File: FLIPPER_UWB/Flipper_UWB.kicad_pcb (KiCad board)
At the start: 2 copper layers, 34 x 67 mm, 13 parts, among them IC1 DWM1000, J1 Conn_01x08_Socket, J2 Conn_01x10_Socket

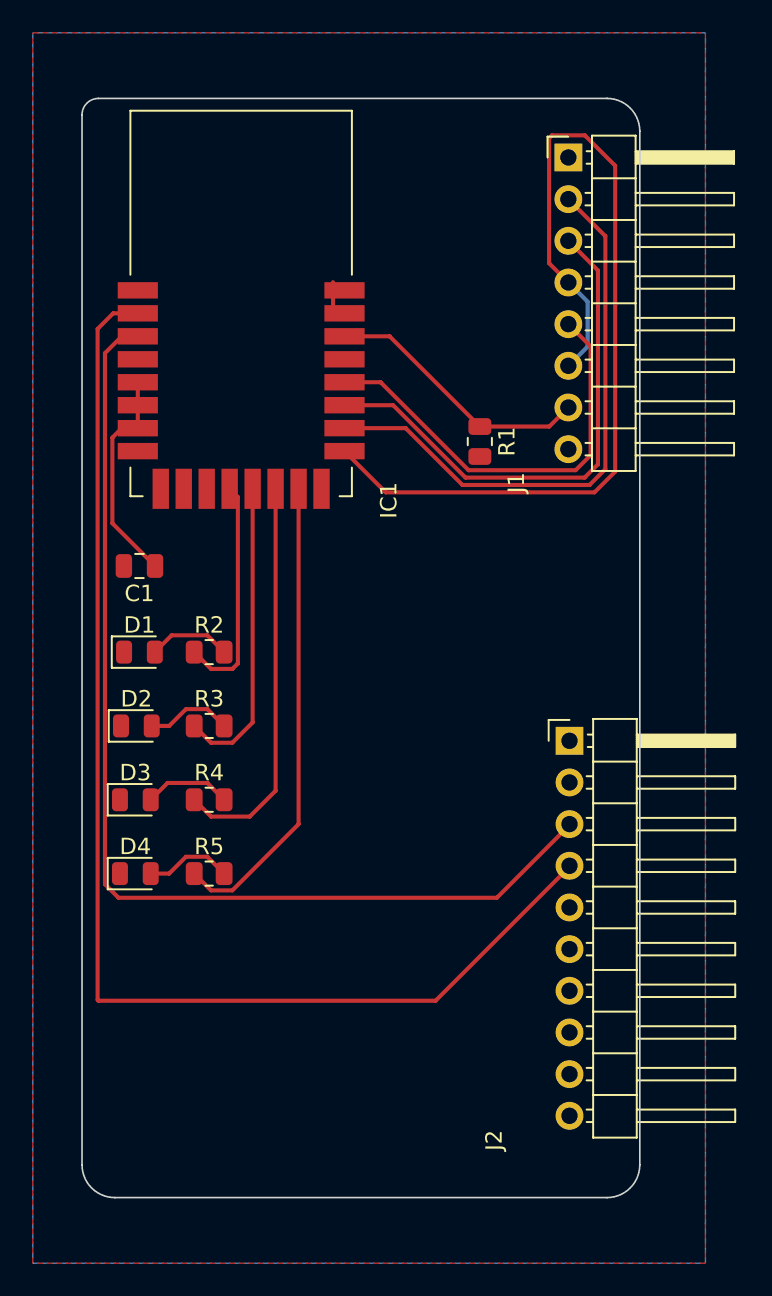
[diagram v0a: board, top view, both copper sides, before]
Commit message: Update Flipper_UWB pcb
Corrected PCB
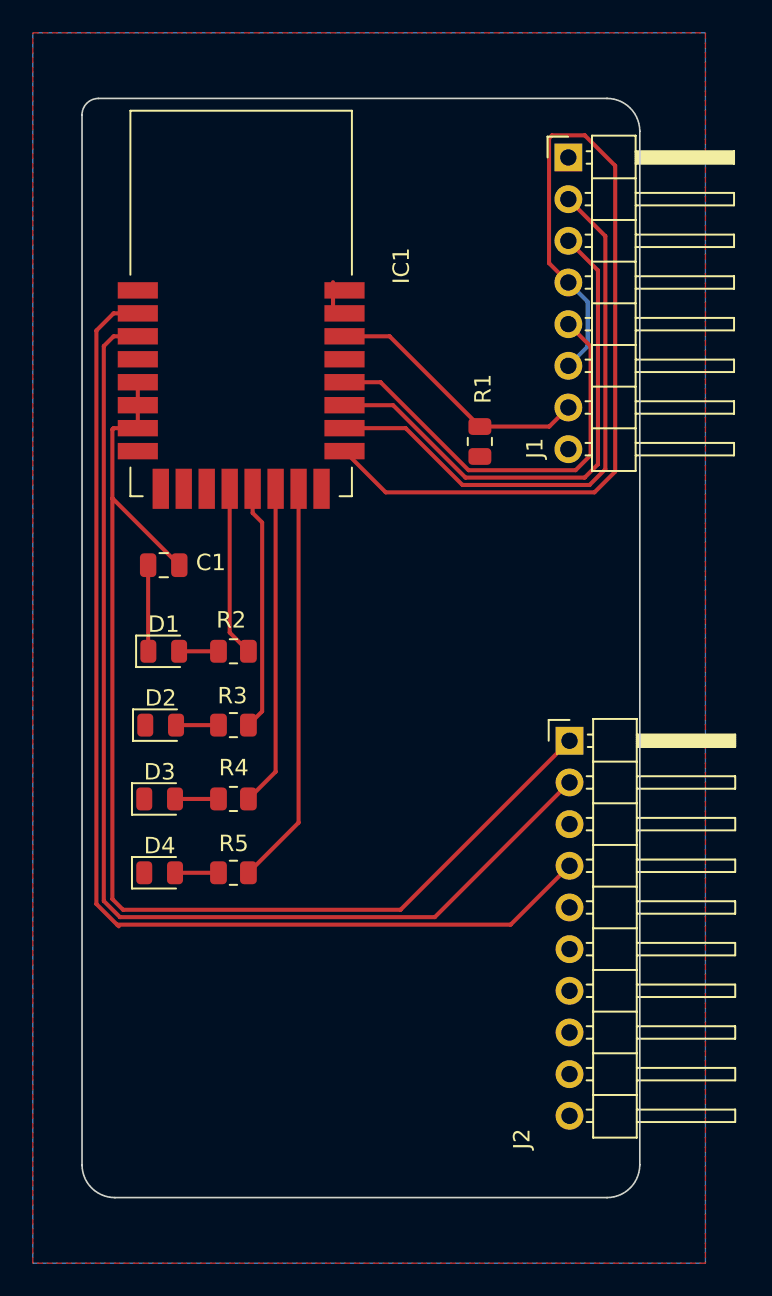
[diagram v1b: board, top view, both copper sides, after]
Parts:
- moved C1 1.48 mm to (129.0, 91.5)
- moved D1 1.48 mm to (129.0, 96.7)
- moved D2 1.48 mm to (128.8, 101.2)
- moved D3 1.48 mm to (128.7, 105.7)
- moved D4 1.48 mm to (128.7, 110.2)
- moved R2 1.48 mm to (133.2, 96.7), turned to 180 degrees
- moved R3 1.48 mm to (133.2, 101.2), turned to 180 degrees
- moved R4 1.48 mm to (133.2, 105.7), turned to 180 degrees
- moved R5 1.48 mm to (133.2, 110.2), turned to 180 degrees
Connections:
- J2 pad 1: unconnected-(J2-Pin_1-Pad1) -> +3.3V
- J2 pad 2: GND -> /RSTN
- J2 pad 3: /RSTN -> GND
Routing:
- net +3.3V: track 13.5 -> 71.2 mm
- net /WKP: track 75.8 -> 68.9 mm
- net GND: track 1.40 -> 6.66 mm
- net /LED3: track 24.4 -> 19.6 mm
- net /LED4: track 28.9 -> 24.7 mm
- net /LED2: track 18.7 -> 15.0 mm
- net /LED1: track 14.1 -> 10.9 mm
- net /RSTN: track 65.2 -> 68.3 mm
- net Net-(D4-A): track 5.32 -> 2.65 mm
- net Net-(D3-A): track 5.32 -> 2.65 mm
- net Net-(D2-A): track 5.26 -> 2.59 mm
- net Net-(D1-A): track 5.07 -> 2.40 mm

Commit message: Update and correction shield UWB
Update and correction of the Flipper Zero UWB shield.
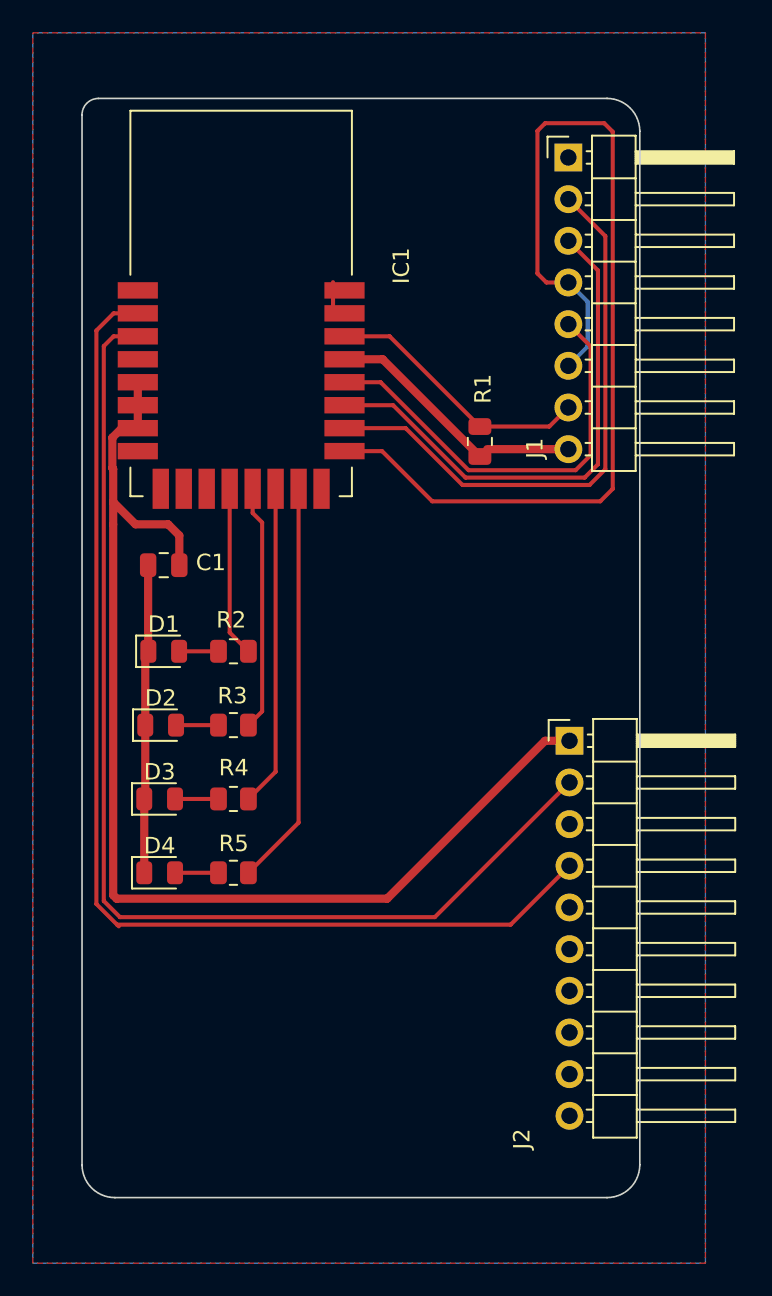
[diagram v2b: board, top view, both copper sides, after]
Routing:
- net GND: track 6.66 -> 36.5 mm
- net /CS: track 56.9 -> 61.6 mm
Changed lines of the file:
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@@
   (segment (start 153.715 104.695) (end 145.504 112.906) (width 0.25) (layer "F.Cu") (net 3))
   (segment (start 125.326 111.918396) (end 125.326 78.099) (width 0.25) (layer "F.Cu") (net 3))
-  (segment (start 127.4 80.3) (end 127.4 81.7) (width 0.25) (layer "F.Cu") (net 5))
-  (segment (start 143.414 112.456) (end 153.715 102.155) (width 0.25) (layer "F.Cu") (net 5))
-  (segment (start 125.85 83.175) (end 125.85 87.37) (width 0.25) (layer "F.Cu") (net 5))
-  (segment (start 125.85 87.37) (end 129.9305 91.4505) (width 0.25) (layer "F.Cu") (net 5))
-  (segment (start 125.925 83.1) (end 125.85 83.175) (width 0.25) (layer "F.Cu") (net 5))
-  (segment (start 126.5 112.456) (end 143.414 112.456) (width 0.25) (layer "F.Cu") (net 5))
-  (segment (start 127.4 81.7) (end 127.4 83.1) (width 0.25) (layer "F.Cu") (net 5))
-  (segment (start 127.4 83.1) (end 125.925 83.1) (width 0.25) (layer "F.Cu") (net 5))
-  (segment (start 125.85 111.806) (end 126.5 112.456) (width 0.25) (layer "F.Cu") (net 5))
-  (segment (start 125.85 87.37) (end 125.85 111.806) (width 0.25) (layer "F.Cu") (net 5))
+  (segment (start 152.225 102.155) (end 142.6 111.78) (width 0.5) (layer "F.Cu") (net 5))
+  (segment (start 126.425 83.1) (end 127.4 83.1) (width 0.5) (layer "F.Cu") (net 5))
+  (segment (start 126.11 111.78) (end 125.9 111.57) (width 0.5) (layer "F.Cu") (net 5))
+  (segment (start 129.9305 89.6405) (end 129.25 88.96) (width 0.5) (layer "F.Cu") (net 5))
+  (segment (start 127.4 80.3) (end 127.4 81.7) (width 0.5) (layer "F.Cu") (net 5))
+  (segment (start 125.85 85.54) (end 125.85 83.675) (width 0.5) (layer "F.Cu") (net 5))
+  (segment (start 125.9 111.57) (end 125.9 88.96) (width 0.5) (layer "F.Cu") (net 5))
+  (segment (start 125.85 83.675) (end 126.425 83.1) (width 0.5) (layer "F.Cu") (net 5))
+  (segment (start 153.715 102.155) (end 152.225 102.155) (width 0.5) (layer "F.Cu") (net 5))
+  (segment (start 129.9305 91.4505) (end 129.9305 89.6405) (width 0.5) (layer "F.Cu") (net 5))
+  (segment (start 142.6 111.78) (end 126.11 111.78) (width 0.5) (layer "F.Cu") (net 5))
+  (segment (start 125.9 85.59) (end 125.85 85.54) (width 0.5) (layer "F.Cu") (net 5))
+  (segment (start 129.25 88.96) (end 127.26 88.96) (width 0.5) (layer "F.Cu") (net 5))
+  (segment (start 127.4 81.7) (end 127.4 83.1) (width 0.5) (layer "F.Cu") (net 5))
+  (segment (start 125.9 88.96) (end 125.9 87.6) (width 0.5) (layer "F.Cu") (net 5))
+  (segment (start 125.9 87.6) (end 125.9 85.59) (width 0.5) (layer "F.Cu") (net 5))
+  (segment (start 127.26 88.96) (end 125.9 87.6) (width 0.5) (layer "F.Cu") (net 5))
+  (segment (start 148.25 84.825) (end 148.6962 84.3788) (width 0.25) (layer "F.Cu") (net 6))
+  (segment (start 148.6962 84.3788) (end 153.6446 84.3788) (width 0.5) (layer "F.Cu") (net 6))
+  (segment (start 140 78.9) (end 142.325 78.9) (width 0.5) (layer "F.Cu") (net 6))
+  (segment (start 127.8555 101.2005) (end 127.8555 105.638) (width 0.5) (layer "F.Cu") (net 6))
+  (segment (start 142.325 78.9) (end 148.25 84.825) (width 0.5) (layer "F.Cu") (net 6))
   (segment (start 128.043 96.7005) (end 128.0305 96.688) (width 0.25) (layer "F.Cu") (net 6))
   (segment (start 139.3 74.2012) (end 139.3 75.6012) (width 0.25) (layer "F.Cu") (net 6))
-  (segment (start 128.0305 96.688) (end 128.0305 91.4505) (width 0.25) (layer "F.Cu") (net 6))
+  (segment (start 127.8555 105.638) (end 127.793 105.7005) (width 0.25) (layer "F.Cu") (net 6))
+  (segment (start 127.793 110.2005) (end 127.793 105.7005) (width 0.5) (layer "F.Cu") (net 6))
+  (segment (start 128.0305 96.688) (end 128.0305 91.4505) (width 0.5) (layer "F.Cu") (net 6))
+  (segment (start 127.8555 96.863) (end 127.8555 101.2005) (width 0.5) (layer "F.Cu") (net 6))
+  (segment (start 128.0305 96.688) (end 127.8555 96.863) (width 0.25) (layer "F.Cu") (net 6))
   (segment (start 129.7305 101.2005) (end 132.318 101.2005) (width 0.25) (layer "F.Cu") (net 10))
   (segment (start 129.668 105.7005) (end 132.318 105.7005) (width 0.25) (layer "F.Cu") (net 11))
@@
   (segment (start 124.876 112.104792) (end 126.239208 113.468) (width 0.25) (layer "F.Cu") (net 13))
   (segment (start 124.876 77.149) (end 124.876 112.104792) (width 0.25) (layer "F.Cu") (net 13))
-  (segment (start 156.5 85.75) (end 156.5 67.1042) (width 0.25) (layer "F.Cu") (net 14))
-  (segment (start 152.4696 65.4238) (end 152.4696 73.0438) (width 0.25) (layer "F.Cu") (net 14))
-  (segment (start 154.6458 65.25) (end 152.6434 65.25) (width 0.25) (layer "F.Cu") (net 14))
-  (segment (start 156.5 67.1042) (end 154.6458 65.25) (width 0.25) (layer "F.Cu") (net 14))
-  (segment (start 152.6434 65.25) (end 152.4696 65.4238) (width 0.25) (layer "F.Cu") (net 14))
-  (segment (start 140 84.4988) (end 142.5137 87.0125) (width 0.25) (layer "F.Cu") (net 14))
-  (segment (start 155.2375 87.0125) (end 156.5 85.75) (width 0.25) (layer "F.Cu") (net 14))
-  (segment (start 142.5137 87.0125) (end 155.2375 87.0125) (width 0.25) (layer "F.Cu") (net 14))
-  (segment (start 152.4696 73.0438) (end 153.6446 74.2188) (width 0.25) (layer "F.Cu") (net 14))
+  (segment (start 155.59 87.56) (end 156.35 86.8) (width 0.25) (layer "F.Cu") (net 14))
+  (segment (start 155.83 64.51) (end 152.23 64.51) (width 0.25) (layer "F.Cu") (net 14))
+  (segment (start 142.2888 84.4988) (end 145.35 87.56) (width 0.25) (layer "F.Cu") (net 14))
+  (segment (start 151.76 73.67) (end 152.3088 74.2188) (width 0.25) (layer "F.Cu") (net 14))
+  (segment (start 140 84.4988) (end 142.2888 84.4988) (width 0.25) (layer "F.Cu") (net 14))
+  (segment (start 145.35 87.56) (end 155.59 87.56) (width 0.25) (layer "F.Cu") (net 14))
+  (segment (start 151.76 64.98) (end 151.76 73.67) (width 0.25) (layer "F.Cu") (net 14))
+  (segment (start 156.35 86.8) (end 156.35 65.03) (width 0.25) (layer "F.Cu") (net 14))
+  (segment (start 152.23 64.51) (end 151.76 64.98) (width 0.25) (layer "F.Cu") (net 14))
+  (segment (start 156.35 65.03) (end 155.83 64.51) (width 0.25) (layer "F.Cu") (net 14))
+  (segment (start 152.3088 74.2188) (end 153.6446 74.2188) (width 0.25) (layer "F.Cu") (net 14))
   (segment (start 153.6446 74.2188) (end 154.8196 75.3938) (width 0.25) (layer "B.Cu") (net 14))
   (segment (start 154.8196 75.3938) (end 154.8196 78.1238) (width 0.25) (layer "B.Cu") (net 14))
@@
   (zone (net 6) (net_name "GND") (layer "F.Cu") (hatch edge 0.5)
     (connect_pads (clearance 0.5))
-    (min_thickness 0.25) (filled_areas_thickness no)
+    (min_thickness 0.5) (filled_areas_thickness no)
     (fill yes (thermal_gap 0.5) (thermal_bridge_width 0.5))
     (polygon

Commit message: Correction of the PCB and the schematic
Correction of the PCB and the schematic of the UBW shield for the FlipperZero
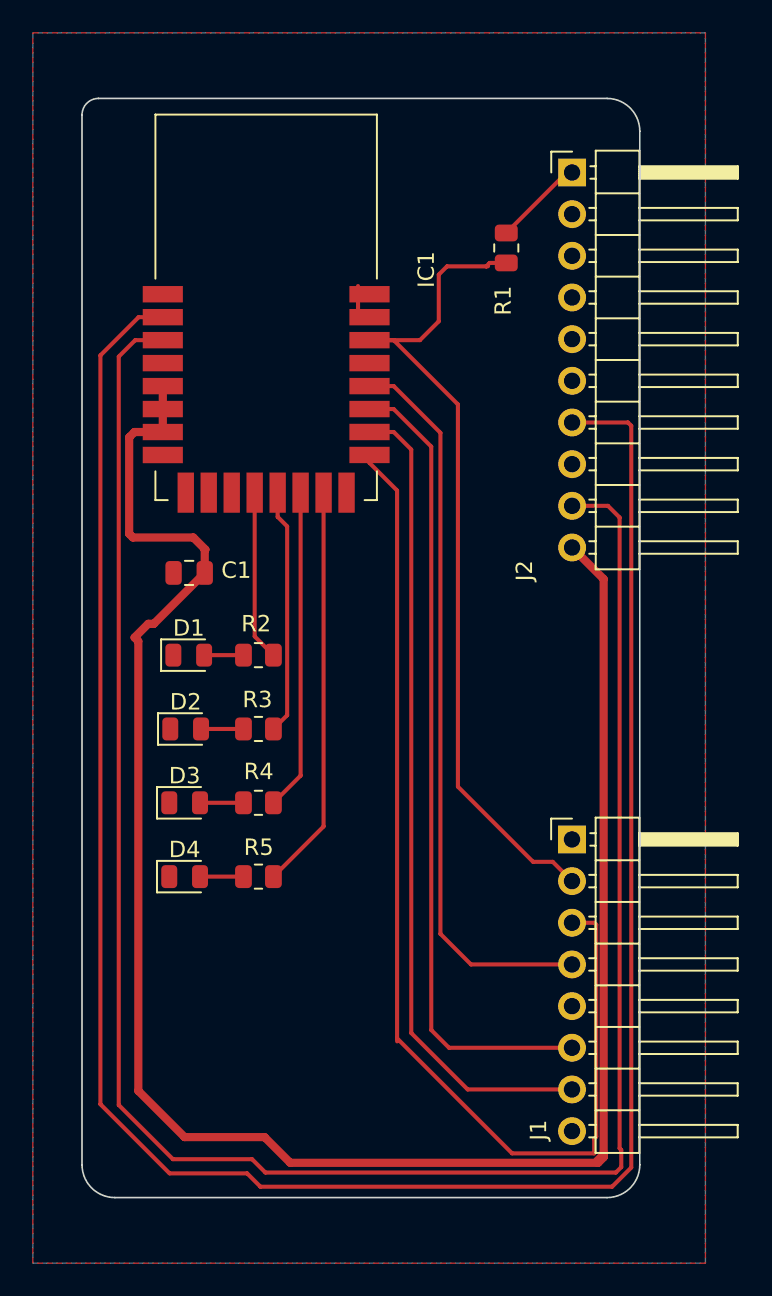
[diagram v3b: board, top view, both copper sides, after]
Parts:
- moved J1 41.6 mm to (153.9, 108.2)
- moved J2 34.6 mm to (153.9, 67.5)
- moved R1 11.9 mm to (149.9, 72.1), turned to 90 degrees
- moved C1 1.62 mm to (130.5, 91.9)
- moved D1 1.54 mm to (130.5, 96.9)
- moved D2 1.54 mm to (130.3, 101.4)
- moved D3 1.54 mm to (130.3, 105.9)
- moved D4 1.54 mm to (130.3, 110.4)
- moved IC1 1.54 mm to (135.2, 75.7)
- moved R2 1.54 mm to (134.8, 96.9)
- moved R3 1.54 mm to (134.8, 101.4)
- moved R4 1.54 mm to (134.8, 105.9)
- moved R5 1.54 mm to (134.8, 110.4)
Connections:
- J1 pad 1: +5V -> GND
- J1 pad 2: /MOSI -> /IRQ
- J1 pad 3: /MISO -> /CS
- J1 pad 4: /CS -> /CLK
- J1 pad 5: /CLK -> unconnected-(J1-Pin_5-Pad5)
- J1 pad 6: /CS -> /MISO
- J1 pad 7: /IRQ -> /MOSI
- J1 pad 8: GND -> +5V
- J2 pad 1: +3.3V -> GND
- J2 pad 10: GND -> +3.3V
- J2 pad 2: /RSTN -> unconnected-(J2-Pin_2-Pad2)
- J2 pad 3: GND -> unconnected-(J2-Pin_3-Pad3)
- J2 pad 4: /WKP -> unconnected-(J2-Pin_4-Pad4)
- J2 pad 7: unconnected-(J2-Pin_7-Pad7) -> /WKP
- J2 pad 8: unconnected-(J2-Pin_8-Pad8) -> GND
- J2 pad 9: unconnected-(J2-Pin_9-Pad9) -> /RSTN
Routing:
- net /WKP: track 68.9 -> 134.2 mm
- net /RSTN: track 68.3 -> 124.0 mm
- net +3.3V: track 71.1 -> 120.0 mm
- net /IRQ: track 16.4 -> 51.7 mm
- net GND: track 36.5 -> 6.55 mm
- net /CLK: track 26.2 -> 44.8 mm
- net /MISO: track 32.0 -> 49.3 mm
- net /MOSI: track 35.1 -> 49.8 mm
- net /CS: track 61.6 -> 66.9 mm

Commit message: Update PCB FLipperZero UWB
Update and correction PCB
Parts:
- added G***: LOGO, Aesthetics:electronic_cats_logo_8x6, F.Cu at (134.0, 118.7)
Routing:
- net /IRQ: track 51.7 -> 54.5 mm
- net /CS: track 66.9 -> 69.2 mm
- net /MOSI: track 49.8 -> 51.3 mm
- net +3.3V: track 120.0 -> 120.9 mm
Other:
- board text added: "FlipperZero UWB Shield"

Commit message: Update Flipper UWB
Update Flipper UWB
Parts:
- added G***: LOGO, Aesthetics:GND, F.Cu at (150.7, 108.0)
- added G***: LOGO, Aesthetics:3v3, F.Cu at (150.8, 90.4)
- added G***: LOGO, Aesthetics:GND, F.Cu at (150.9, 67.5)
- added G***: LOGO, Aesthetics:GND, F.Cu at (150.9, 85.3)
- added kibuzzard-644981B9: G***, kibuzzard-644981B9, F.Cu at (150.5, 120.8)
- added kibuzzard-644981FD: G***, kibuzzard-644981FD, F.Cu at (150.5, 123.4)
- added kibuzzard-64498233: G***, kibuzzard-64498233, F.Cu at (151.0, 115.8)
- added kibuzzard-64498280: G***, kibuzzard-64498280, F.Cu at (151.0, 113.2)
- added kibuzzard-644982A0: G***, kibuzzard-644982A0, F.Cu at (150.8, 110.6)
- added kibuzzard-644982E2: G***, kibuzzard-644982E2, F.Cu at (150.9, 82.8)
- added kibuzzard-644982F5: G***, kibuzzard-644982F5, F.Cu at (150.9, 87.8)
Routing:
- net /IRQ: track 54.5 -> 53.0 mm
- net /WKP: track 134.2 -> 135.4 mm
- net /RSTN: track 124.0 -> 124.7 mm
- net /CLK: track 44.8 -> 45.5 mm
- net /MISO: track 49.3 -> 49.9 mm
- net /CS: track 69.2 -> 69.8 mm
- net +3.3V: track 120.9 -> 121.5 mm

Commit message: Update PCB UWB
Update shield UWB
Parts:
- moved C1 2.16 mm to (128.4, 92.3), turned to 0 degrees
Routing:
- net +3.3V: track 121.5 -> 114.6 mm
- net GND: track 6.55 -> 1.67 mm
- net /IRQ: track 53.0 -> 52.0 mm
- net /CS: track 69.8 -> 70.4 mm
